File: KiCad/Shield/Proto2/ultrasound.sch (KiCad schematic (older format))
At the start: 38 parts, among them J10 CONN_01X02, J11 CONN_01X02, J3 CONN_01X02, J4 CONN_01X02, J5 CONN_01X02, J6 CONN_01X02, J8 CONN_01X02, J9 CONN_01X02, Q1 BFY51, Q2 BFY51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

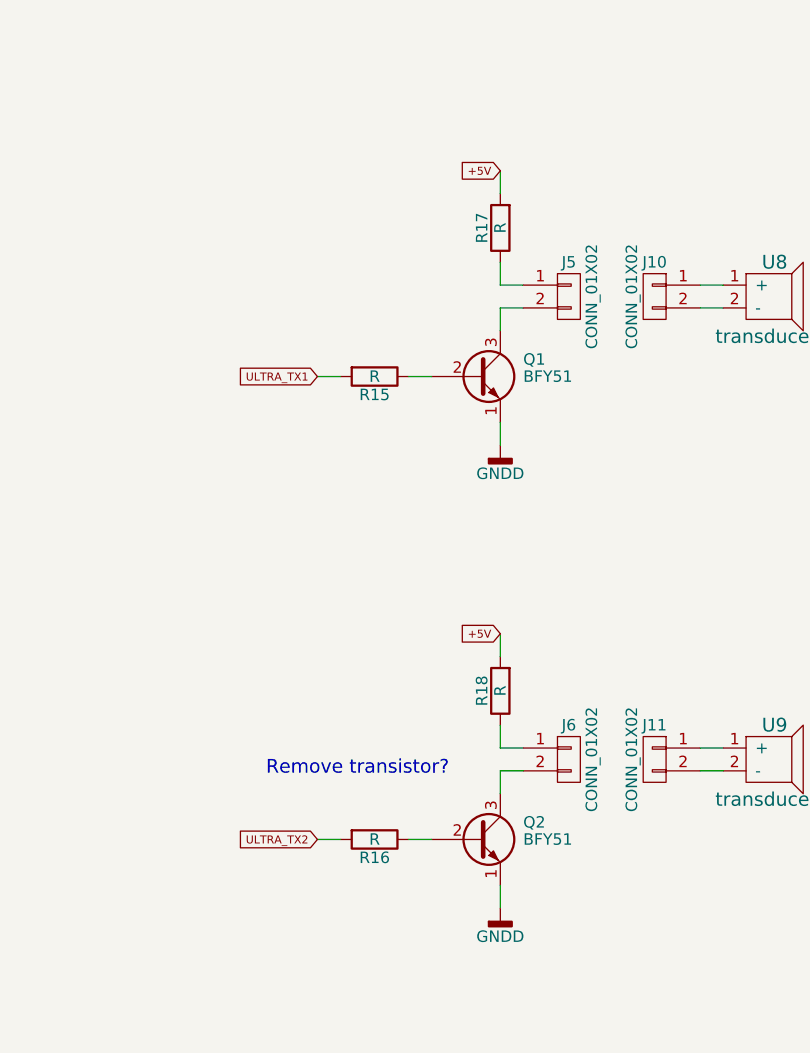
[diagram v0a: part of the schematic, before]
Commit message: Added proto2 kicad files
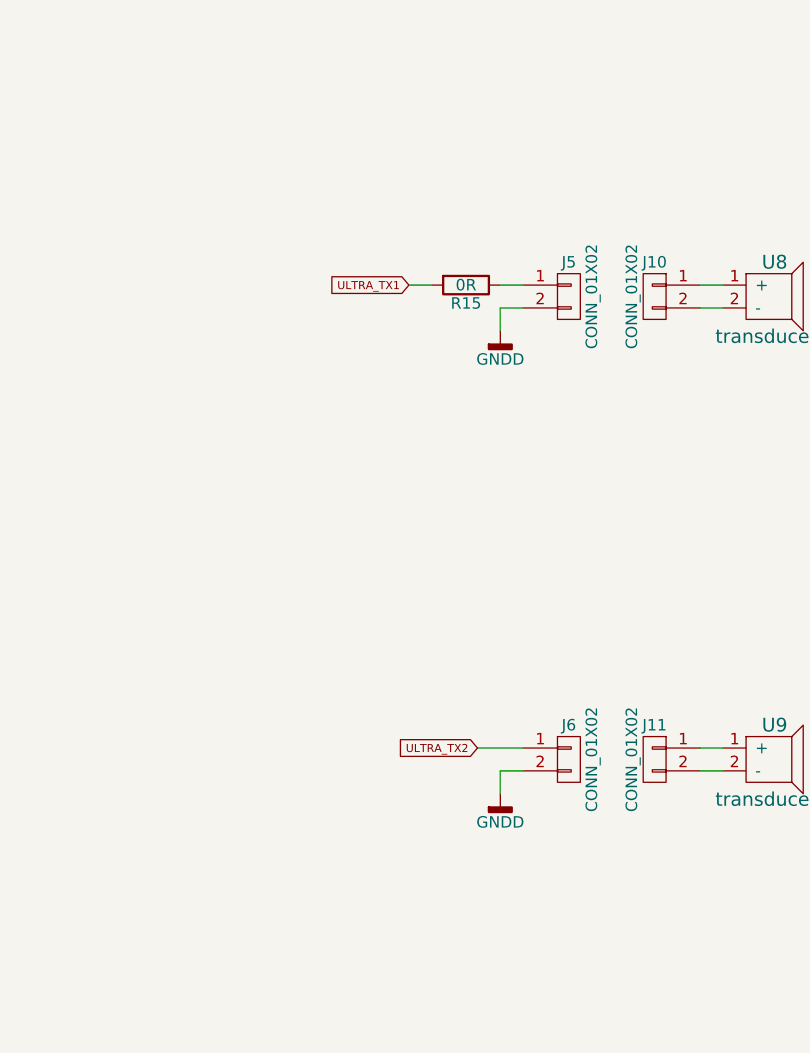
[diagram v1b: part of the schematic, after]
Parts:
- removed Q1, Q2: BFY51, TO_SOT_Packages_THT:TO-92_Molded_Narrow, symbol 2N3904
- removed R16, R17, R18: R, Resistors_THT:R_Axial_DIN0207_L6.3mm_D2.5mm_P10.16mm_Horizontal, symbol R
- R15: value R -> 0R; part# UofG -> (none)
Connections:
- net GNDD: now also J5.2 (P2), J6.2 (P2)
- net ULTRA_TX2: now also J6.1 (P1)
- net at R15.1: now also J5.1 (P1)
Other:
- note removed: "Remove transistor?"
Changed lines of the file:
@@
 $EndDescr
-$Comp
-L 2N3904 Q1
-U 1 1 5AA6BA04
-P 8925 2500
-F 0 "Q1" H 9125 2575 50  0000 L CNN
-F 1 "BFY51" H 9125 2500 50  0000 L CNN
-F 2 "TO_SOT_Packages_THT:TO-92_Molded_Narrow" H 9125 2425 50  0001 L CIN
-F 3 "" H 8925 2500 50  0001 L CNN
-F 4 "UofG" H 9125 2675 50  0001 C CNN "part#"
-	1    8925 2500
-	1    0    0    -1
-$EndComp
-$Comp
-L R R15
-U 1 1 5AA6BAAA
-P 8475 2500
-F 0 "R15" V 8555 2500 50  0000 C CNN
-F 1 "R" V 8475 2500 50  0000 C CNN
-F 2 "Resistors_THT:R_Axial_DIN0207_L6.3mm_D2.5mm_P10.16mm_Horizontal" V 8405 2500 50  0001 C CNN
-F 3 "" H 8475 2500 50  0001 C CNN
-F 4 "UofG" H 8555 2600 50  0001 C CNN "part#"
-	1    8475 2500
-	0    1    1    0
-$EndComp
 $Comp
 L CONN_01X02 J5
@@
 $EndComp
 $Comp
-L GNDD #PWR018
+L GNDD #PWR21
 U 1 1 5AA6C525
 P 2000 1900
-F 0 "#PWR018" H 2000 1650 50  0001 C CNN
+F 0 "#PWR21" H 2000 1650 50  0001 C CNN
 F 1 "GNDD" H 2000 1775 50  0000 C CNN
 F 2 "" H 2000 1900 50  0001 C CNN
@@
 $EndComp
 $Comp
-L GNDD #PWR019
+L GNDD #PWR23
 U 1 1 5AA6C8C0
 P 3200 2200
-F 0 "#PWR019" H 3200 1950 50  0001 C CNN
+F 0 "#PWR23" H 3200 1950 50  0001 C CNN
 F 1 "GNDD" H 3200 2075 50  0000 C CNN
 F 2 "" H 3200 2200 50  0001 C CNN
@@
 $EndComp
 $Comp
-L GNDD #PWR020
+L GNDD #PWR25
 U 1 1 5AA6CAA3
 P 3650 2825
-F 0 "#PWR020" H 3650 2575 50  0001 C CNN
+F 0 "#PWR25" H 3650 2575 50  0001 C CNN
 F 1 "GNDD" H 3650 2700 50  0000 C CNN
 F 2 "" H 3650 2825 50  0001 C CNN
@@
 $EndComp
 $Comp
-L GNDD #PWR022
+L GNDD #PWR22
 U 1 1 5AA6EB7C
 P 2000 4275
-F 0 "#PWR022" H 2000 4025 50  0001 C CNN
+F 0 "#PWR22" H 2000 4025 50  0001 C CNN
 F 1 "GNDD" H 2000 4150 50  0000 C CNN
 F 2 "" H 2000 4275 50  0001 C CNN
@@
 $EndComp
 $Comp
-L GNDD #PWR023
+L GNDD #PWR24
 U 1 1 5AA6EB9A
 P 3200 4575
-F 0 "#PWR023" H 3200 4325 50  0001 C CNN
+F 0 "#PWR24" H 3200 4325 50  0001 C CNN
 F 1 "GNDD" H 3200 4450 50  0000 C CNN
 F 2 "" H 3200 4575 50  0001 C CNN
@@
 $EndComp
 $Comp
-L GNDD #PWR024
+L GNDD #PWR26
 U 1 1 5AA6EBB3
 P 3650 5200
-F 0 "#PWR024" H 3650 4950 50  0001 C CNN
+F 0 "#PWR26" H 3650 4950 50  0001 C CNN
 F 1 "GNDD" H 3650 5075 50  0000 C CNN
 F 2 "" H 3650 5200 50  0001 C CNN
@@
 $EndComp
 $Comp
-L GNDD #PWR026
+L GNDD #PWR29
 U 1 1 5AA71D20
 P 5350 2050
-F 0 "#PWR026" H 5350 1800 50  0001 C CNN
+F 0 "#PWR29" H 5350 1800 50  0001 C CNN
 F 1 "GNDD" H 5350 1925 50  0000 C CNN
 F 2 "" H 5350 2050 50  0001 C CNN
@@
 $EndComp
 $Comp
-L GNDD #PWR027
+L GNDD #PWR30
 U 1 1 5AA72560
 P 5350 4425
-F 0 "#PWR027" H 5350 4175 50  0001 C CNN
+F 0 "#PWR30" H 5350 4175 50  0001 C CNN
 F 1 "GNDD" H 5350 4300 50  0000 C CNN
 F 2 "" H 5350 4425 50  0001 C CNN
@@
 $EndComp
 $Comp
-L GNDD #PWR028
+L GNDD #PWR18
 U 1 1 5AA740D9
 P 725 1050
-F 0 "#PWR028" H 725 800 50  0001 C CNN
+F 0 "#PWR18" H 725 800 50  0001 C CNN
 F 1 "GNDD" H 725 925 50  0000 C CNN
 F 2 "" H 725 1050 50  0001 C CNN
@@
 	1    725  1050
 	1    0    0    -1
-$EndComp
-$Comp
-L 2N3904 Q2
-U 1 1 5AA7825F
-P 8925 4525
-F 0 "Q2" H 9125 4600 50  0000 L CNN
-F 1 "BFY51" H 9125 4525 50  0000 L CNN
-F 2 "TO_SOT_Packages_THT:TO-92_Molded_Narrow" H 9125 4450 50  0001 L CIN
-F 3 "" H 8925 4525 50  0001 L CNN
-F 4 "UofG" H 9125 4700 50  0001 C CNN "part#"
-	1    8925 4525
-	1    0    0    -1
-$EndComp
-$Comp
-L R R16
-U 1 1 5AA78266
-P 8475 4525
-F 0 "R16" V 8555 4525 50  0000 C CNN
-F 1 "R" V 8475 4525 50  0000 C CNN
-F 2 "Resistors_THT:R_Axial_DIN0207_L6.3mm_D2.5mm_P10.16mm_Horizontal" V 8405 4525 50  0001 C CNN
-F 3 "" H 8475 4525 50  0001 C CNN
-F 4 "UofG" H 8555 4625 50  0001 C CNN "part#"
-	1    8475 4525
-	0    1    1    0
 $EndComp
 $Comp
@@
 $EndComp
 $Comp
-L GNDD #PWR029
+L GNDD #PWR34
 U 1 1 5AA7C06F
 P 6250 5075
-F 0 "#PWR029" H 6250 4825 50  0001 C CNN
+F 0 "#PWR34" H 6250 4825 50  0001 C CNN
 F 1 "GNDD" H 6250 4950 50  0000 C CNN
 F 2 "" H 6250 5075 50  0001 C CNN
@@
 $EndComp
 $Comp
-L GNDD #PWR030
+L GNDD #PWR33
 U 1 1 5AA7C60E
 P 6250 2700
-F 0 "#PWR030" H 6250 2450 50  0001 C CNN
+F 0 "#PWR33" H 6250 2450 50  0001 C CNN
 F 1 "GNDD" H 6250 2575 50  0000 C CNN
 F 2 "" H 6250 2700 50  0001 C CNN
@@
 $EndComp
 $Comp
-L GNDD #PWR031
+L GNDD #PWR35
 U 1 1 5AA7D3DC
-P 9025 2800
-F 0 "#PWR031" H 9025 2550 50  0001 C CNN
-F 1 "GNDD" H 9025 2675 50  0000 C CNN
-F 2 "" H 9025 2800 50  0001 C CNN
-F 3 "" H 9025 2800 50  0001 C CNN
-	1    9025 2800
-	1    0    0    -1
-$EndComp
-$Comp
-L GNDD #PWR032
+P 9025 2300
+F 0 "#PWR35" H 9025 2050 50  0001 C CNN
+F 1 "GNDD" H 9025 2175 50  0000 C CNN
+F 2 "" H 9025 2300 50  0001 C CNN
+F 3 "" H 9025 2300 50  0001 C CNN
+	1    9025 2300
+	1    0    0    -1
+$EndComp
+$Comp
+L GNDD #PWR36
 U 1 1 5AA7D4D7
-P 9025 4825
-F 0 "#PWR032" H 9025 4575 50  0001 C CNN
-F 1 "GNDD" H 9025 4700 50  0000 C CNN
-F 2 "" H 9025 4825 50  0001 C CNN
-F 3 "" H 9025 4825 50  0001 C CNN
-	1    9025 4825
-	1    0    0    -1
-$EndComp
-$Comp
-L R R17
-U 1 1 5AA7DC76
-P 9025 1850
-F 0 "R17" V 9105 1850 50  0000 C CNN
-F 1 "R" V 9025 1850 50  0000 C CNN
-F 2 "Resistors_THT:R_Axial_DIN0207_L6.3mm_D2.5mm_P10.16mm_Horizontal" V 8955 1850 50  0001 C CNN
-F 3 "" H 9025 1850 50  0001 C CNN
-F 4 "UofG" H 9105 1950 50  0001 C CNN "part#"
-	1    9025 1850
-	-1   0    0    1
-$EndComp
-$Comp
-L R R18
-U 1 1 5AA7E759
-P 9025 3875
-F 0 "R18" V 9105 3875 50  0000 C CNN
-F 1 "R" V 9025 3875 50  0000 C CNN
-F 2 "Resistors_THT:R_Axial_DIN0207_L6.3mm_D2.5mm_P10.16mm_Horizontal" V 8955 3875 50  0001 C CNN
-F 3 "" H 9025 3875 50  0001 C CNN
-F 4 "UofG" H 9105 3975 50  0001 C CNN "part#"
-	1    9025 3875
-	-1   0    0    1
+P 9025 4325
+F 0 "#PWR36" H 9025 4075 50  0001 C CNN
+F 1 "GNDD" H 9025 4200 50  0000 C CNN
+F 2 "" H 9025 4325 50  0001 C CNN
+F 3 "" H 9025 4325 50  0001 C CNN
+	1    9025 4325
+	1    0    0    -1
 $EndComp
 $Comp
@@
 $EndComp
 $Comp
-L GNDD #PWR033
+L GNDD #PWR20
 U 1 1 5AABF5D3
 P 1050 4275
-F 0 "#PWR033" H 1050 4025 50  0001 C CNN
+F 0 "#PWR20" H 1050 4025 50  0001 C CNN
 F 1 "GNDD" H 1050 4150 50  0000 C CNN
 F 2 "" H 1050 4275 50  0001 C CNN
@@
 $EndComp
 $Comp
-L GNDD #PWR034
+L GNDD #PWR19
 U 1 1 5AAC33E8
 P 1050 1900
-F 0 "#PWR034" H 1050 1650 50  0001 C CNN
+F 0 "#PWR19" H 1050 1650 50  0001 C CNN
 F 1 "GNDD" H 1050 1775 50  0000 C CNN
 F 2 "" H 1050 1900 50  0001 C CNN
@@
 $EndComp
 $Comp
-L GNDD #PWR035
+L GNDD #PWR28
 U 1 1 5AAB16DC
 P 3825 2150
-F 0 "#PWR035" H 3825 1900 50  0001 C CNN
+F 0 "#PWR28" H 3825 1900 50  0001 C CNN
 F 1 "GNDD" H 3825 2025 50  0000 C CNN
 F 2 "" H 3825 2150 50  0001 C CNN
@@
 $EndComp
 $Comp
-L GNDD #PWR036
+L GNDD #PWR31
 U 1 1 5AAB2119
 P 5475 1525
-F 0 "#PWR036" H 5475 1275 50  0001 C CNN
+F 0 "#PWR31" H 5475 1275 50  0001 C CNN
 F 1 "GNDD" H 5475 1400 50  0000 C CNN
 F 2 "" H 5475 1525 50  0001 C CNN
@@
 $EndComp
 $Comp
-L GNDD #PWR037
+L GNDD #PWR27
 U 1 1 5AAB2A4C
 P 3800 4525
-F 0 "#PWR037" H 3800 4275 50  0001 C CNN
+F 0 "#PWR27" H 3800 4275 50  0001 C CNN
 F 1 "GNDD" H 3800 4400 50  0000 C CNN
 F 2 "" H 3800 4525 50  0001 C CNN
@@
 $EndComp
 $Comp
-L GNDD #PWR038
+L GNDD #PWR32
 U 1 1 5AAB2E03
 P 5475 3900
-F 0 "#PWR038" H 5475 3650 50  0001 C CNN
+F 0 "#PWR32" H 5475 3650 50  0001 C CNN
 F 1 "GNDD" H 5475 3775 50  0000 C CNN
 F 2 "" H 5475 3900 50  0001 C CNN
@@
 	1    0    0    -1
 $EndComp
-Text GLabel 9025 1600 0    35   Input ~ 0
-+5V
-Text GLabel 8225 2500 0    35   Input ~ 0
+Text GLabel 8625 2100 0    35   Input ~ 0
 ULTRA_TX1
 Text GLabel 2100 1700 2    35   Input ~ 0
@@
 Text GLabel 5600 4625 0    35   Input ~ 0
 V_amp+
-Text GLabel 9025 3625 0    35   Input ~ 0
-+5V
-Text GLabel 8225 4525 0    35   Input ~ 0
+Text GLabel 8925 4125 0    35   Input ~ 0
 ULTRA_TX2
 Text GLabel 6350 2300 2    35   Input ~ 0
@@
 ULTRA_RX2_RAW
 Wire Wire Line
-	9025 2700 9025 2800
-Wire Wire Line
-	8325 2500 8225 2500
-Wire Wire Line
-	8625 2500 8725 2500
-Wire Wire Line
 	1900 1700 2100 1700
 Wire Wire Line
@@
 	5650 4625 5600 4625
 Wire Wire Line
-	9025 4725 9025 4825
-Wire Wire Line
-	8325 4525 8225 4525
-Wire Wire Line
-	8625 4525 8725 4525
+	8925 4125 9125 4125
 Wire Wire Line
 	6250 1900 6250 1950
@@
 	9125 4225 9025 4225
 Wire Wire Line
-	9025 3725 9025 3625
-Wire Wire Line
-	9025 4025 9025 4125
-Wire Wire Line
-	9025 4125 9125 4125
-Wire Wire Line
-	9025 4225 9025 4325
-Wire Wire Line
 	9125 2200 9025 2200
-Wire Wire Line
-	9025 2200 9025 2300
-Wire Wire Line
-	9025 2100 9125 2100
-Wire Wire Line
-	9025 2000 9025 2100
-Wire Wire Line
-	9025 1600 9025 1700
 Connection ~ 3200 1700
 Connection ~ 3650 2325
@@
 Text Notes 4350 3525 0    60   ~ 0
 INCREASE GAIN!
-Text Notes 8000 4250 0    60   ~ 0
-Remove transistor?
+Wire Wire Line
+	9025 4225 9025 4325
+Wire Wire Line
+	9025 2200 9025 2300
+$Comp
+L R R15
+U 1 1 5ACB100D
+P 8875 2100
+F 0 "R15" V 8955 2100 50  0000 C CNN
+F 1 "0R" V 8875 2100 50  0000 C CNN
+F 2 "Resistors_THT:R_Axial_DIN0207_L6.3mm_D2.5mm_P10.16mm_Horizontal" V 8805 2100 50  0001 C CNN
+F 3 "" H 8875 2100 50  0001 C CNN
+	1    8875 2100
+	0    1    1    0
+$EndComp
+Wire Wire Line
+	8725 2100 8625 2100
+Wire Wire Line
+	9025 2100 9125 2100
 $EndSCHEMATC

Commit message: Added pdfs of proto2
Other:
- note removed: "INCREASE GAIN!"
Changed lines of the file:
@@
 $EndComp
 $Comp
-L GNDD #PWR21
+L GNDD #PWR018
 U 1 1 5AA6C525
 P 2000 1900
-F 0 "#PWR21" H 2000 1650 50  0001 C CNN
+F 0 "#PWR018" H 2000 1650 50  0001 C CNN
 F 1 "GNDD" H 2000 1775 50  0000 C CNN
 F 2 "" H 2000 1900 50  0001 C CNN
@@
 $EndComp
 $Comp
-L GNDD #PWR23
+L GNDD #PWR019
 U 1 1 5AA6C8C0
 P 3200 2200
-F 0 "#PWR23" H 3200 1950 50  0001 C CNN
+F 0 "#PWR019" H 3200 1950 50  0001 C CNN
 F 1 "GNDD" H 3200 2075 50  0000 C CNN
 F 2 "" H 3200 2200 50  0001 C CNN
@@
 $EndComp
 $Comp
-L GNDD #PWR25
+L GNDD #PWR020
 U 1 1 5AA6CAA3
 P 3650 2825
-F 0 "#PWR25" H 3650 2575 50  0001 C CNN
+F 0 "#PWR020" H 3650 2575 50  0001 C CNN
 F 1 "GNDD" H 3650 2700 50  0000 C CNN
 F 2 "" H 3650 2825 50  0001 C CNN
@@
 $EndComp
 $Comp
-L GNDD #PWR22
+L GNDD #PWR021
 U 1 1 5AA6EB7C
 P 2000 4275
-F 0 "#PWR22" H 2000 4025 50  0001 C CNN
+F 0 "#PWR021" H 2000 4025 50  0001 C CNN
 F 1 "GNDD" H 2000 4150 50  0000 C CNN
 F 2 "" H 2000 4275 50  0001 C CNN
@@
 $EndComp
 $Comp
-L GNDD #PWR24
+L GNDD #PWR022
 U 1 1 5AA6EB9A
 P 3200 4575
-F 0 "#PWR24" H 3200 4325 50  0001 C CNN
+F 0 "#PWR022" H 3200 4325 50  0001 C CNN
 F 1 "GNDD" H 3200 4450 50  0000 C CNN
 F 2 "" H 3200 4575 50  0001 C CNN
@@
 $EndComp
 $Comp
-L GNDD #PWR26
+L GNDD #PWR023
 U 1 1 5AA6EBB3
 P 3650 5200
-F 0 "#PWR26" H 3650 4950 50  0001 C CNN
+F 0 "#PWR023" H 3650 4950 50  0001 C CNN
 F 1 "GNDD" H 3650 5075 50  0000 C CNN
 F 2 "" H 3650 5200 50  0001 C CNN
@@
 $EndComp
 $Comp
-L GNDD #PWR29
+L GNDD #PWR024
 U 1 1 5AA71D20
 P 5350 2050
-F 0 "#PWR29" H 5350 1800 50  0001 C CNN
+F 0 "#PWR024" H 5350 1800 50  0001 C CNN
 F 1 "GNDD" H 5350 1925 50  0000 C CNN
 F 2 "" H 5350 2050 50  0001 C CNN
@@
 $EndComp
 $Comp
-L GNDD #PWR30
+L GNDD #PWR025
 U 1 1 5AA72560
 P 5350 4425
-F 0 "#PWR30" H 5350 4175 50  0001 C CNN
+F 0 "#PWR025" H 5350 4175 50  0001 C CNN
 F 1 "GNDD" H 5350 4300 50  0000 C CNN
 F 2 "" H 5350 4425 50  0001 C CNN
@@
 $EndComp
 $Comp
-L GNDD #PWR18
+L GNDD #PWR026
 U 1 1 5AA740D9
 P 725 1050
-F 0 "#PWR18" H 725 800 50  0001 C CNN
+F 0 "#PWR026" H 725 800 50  0001 C CNN
 F 1 "GNDD" H 725 925 50  0000 C CNN
 F 2 "" H 725 1050 50  0001 C CNN
@@
 $EndComp
 $Comp
-L GNDD #PWR34
+L GNDD #PWR027
 U 1 1 5AA7C06F
 P 6250 5075
-F 0 "#PWR34" H 6250 4825 50  0001 C CNN
+F 0 "#PWR027" H 6250 4825 50  0001 C CNN
 F 1 "GNDD" H 6250 4950 50  0000 C CNN
 F 2 "" H 6250 5075 50  0001 C CNN
@@
 $EndComp
 $Comp
-L GNDD #PWR33
+L GNDD #PWR028
 U 1 1 5AA7C60E
 P 6250 2700
-F 0 "#PWR33" H 6250 2450 50  0001 C CNN
+F 0 "#PWR028" H 6250 2450 50  0001 C CNN
 F 1 "GNDD" H 6250 2575 50  0000 C CNN
 F 2 "" H 6250 2700 50  0001 C CNN
@@
 $EndComp
 $Comp
-L GNDD #PWR35
+L GNDD #PWR029
 U 1 1 5AA7D3DC
 P 9025 2300
-F 0 "#PWR35" H 9025 2050 50  0001 C CNN
+F 0 "#PWR029" H 9025 2050 50  0001 C CNN
 F 1 "GNDD" H 9025 2175 50  0000 C CNN
 F 2 "" H 9025 2300 50  0001 C CNN
@@
 $EndComp
 $Comp
-L GNDD #PWR36
+L GNDD #PWR030
 U 1 1 5AA7D4D7
 P 9025 4325
-F 0 "#PWR36" H 9025 4075 50  0001 C CNN
+F 0 "#PWR030" H 9025 4075 50  0001 C CNN
 F 1 "GNDD" H 9025 4200 50  0000 C CNN
 F 2 "" H 9025 4325 50  0001 C CNN
@@
 $EndComp
 $Comp
-L GNDD #PWR20
+L GNDD #PWR031
 U 1 1 5AABF5D3
 P 1050 4275
-F 0 "#PWR20" H 1050 4025 50  0001 C CNN
+F 0 "#PWR031" H 1050 4025 50  0001 C CNN
 F 1 "GNDD" H 1050 4150 50  0000 C CNN
 F 2 "" H 1050 4275 50  0001 C CNN
@@
 $EndComp
 $Comp
-L GNDD #PWR19
+L GNDD #PWR032
 U 1 1 5AAC33E8
 P 1050 1900
-F 0 "#PWR19" H 1050 1650 50  0001 C CNN
+F 0 "#PWR032" H 1050 1650 50  0001 C CNN
 F 1 "GNDD" H 1050 1775 50  0000 C CNN
 F 2 "" H 1050 1900 50  0001 C CNN
@@
 $EndComp
 $Comp
-L GNDD #PWR28
+L GNDD #PWR033
 U 1 1 5AAB16DC
 P 3825 2150
-F 0 "#PWR28" H 3825 1900 50  0001 C CNN
+F 0 "#PWR033" H 3825 1900 50  0001 C CNN
 F 1 "GNDD" H 3825 2025 50  0000 C CNN
 F 2 "" H 3825 2150 50  0001 C CNN
@@
 $EndComp
 $Comp
-L GNDD #PWR31
+L GNDD #PWR034
 U 1 1 5AAB2119
 P 5475 1525
-F 0 "#PWR31" H 5475 1275 50  0001 C CNN
+F 0 "#PWR034" H 5475 1275 50  0001 C CNN
 F 1 "GNDD" H 5475 1400 50  0000 C CNN
 F 2 "" H 5475 1525 50  0001 C CNN
@@
 $EndComp
 $Comp
-L GNDD #PWR27
+L GNDD #PWR035
 U 1 1 5AAB2A4C
 P 3800 4525
-F 0 "#PWR27" H 3800 4275 50  0001 C CNN
+F 0 "#PWR035" H 3800 4275 50  0001 C CNN
 F 1 "GNDD" H 3800 4400 50  0000 C CNN
 F 2 "" H 3800 4525 50  0001 C CNN
@@
 $EndComp
 $Comp
-L GNDD #PWR32
+L GNDD #PWR036
 U 1 1 5AAB2E03
 P 5475 3900
-F 0 "#PWR32" H 5475 3650 50  0001 C CNN
+F 0 "#PWR036" H 5475 3650 50  0001 C CNN
 F 1 "GNDD" H 5475 3775 50  0000 C CNN
 F 2 "" H 5475 3900 50  0001 C CNN
@@
 Connection ~ 1050 1700
 Connection ~ 1050 4075
-Text Notes 4350 3525 0    60   ~ 0
-INCREASE GAIN!
 Wire Wire Line
 	9025 4225 9025 4325

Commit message: Finished proto2 board
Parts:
- removed C14, C15: 10pF, Capacitors_THT:C_Rect_L7.2mm_W3.0mm_P5.00mm_FKS2_FKP2_MKS2_MKP2, symbol C_Small
- removed R11, R12, R13, R14: R, Resistors_THT:R_Axial_DIN0207_L6.3mm_D2.5mm_P10.16mm_Horizontal, symbol R
- added D1, D2, D3, D4: BAT48, Diodes_THT:D_T-1_P10.16mm_Horizontal, symbol D_Schottky
- R10, R5, R6, R9: value 100K -> 500K
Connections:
- net GNDD: now also D2.2 (A), D4.2 (A)
- net ULTRA_RX1: now also R9.1, U5.14, D1.2 (A), D2.1 (K)
- net ULTRA_RX2: now also R10.1, U5.8, D3.2 (A), D4.1 (K)
- new net +3V3: D1.1 (K), D3.1 (K)
